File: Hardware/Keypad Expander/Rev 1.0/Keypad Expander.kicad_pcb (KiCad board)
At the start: 2 copper layers, 81.8 x 57.6 mm, 18 parts, among them J1 6502 Card Edge, J2 PORT B, J3 PORT A, U1 65C21, U2 AT28C64, U3 74HC138, U4 74HC138

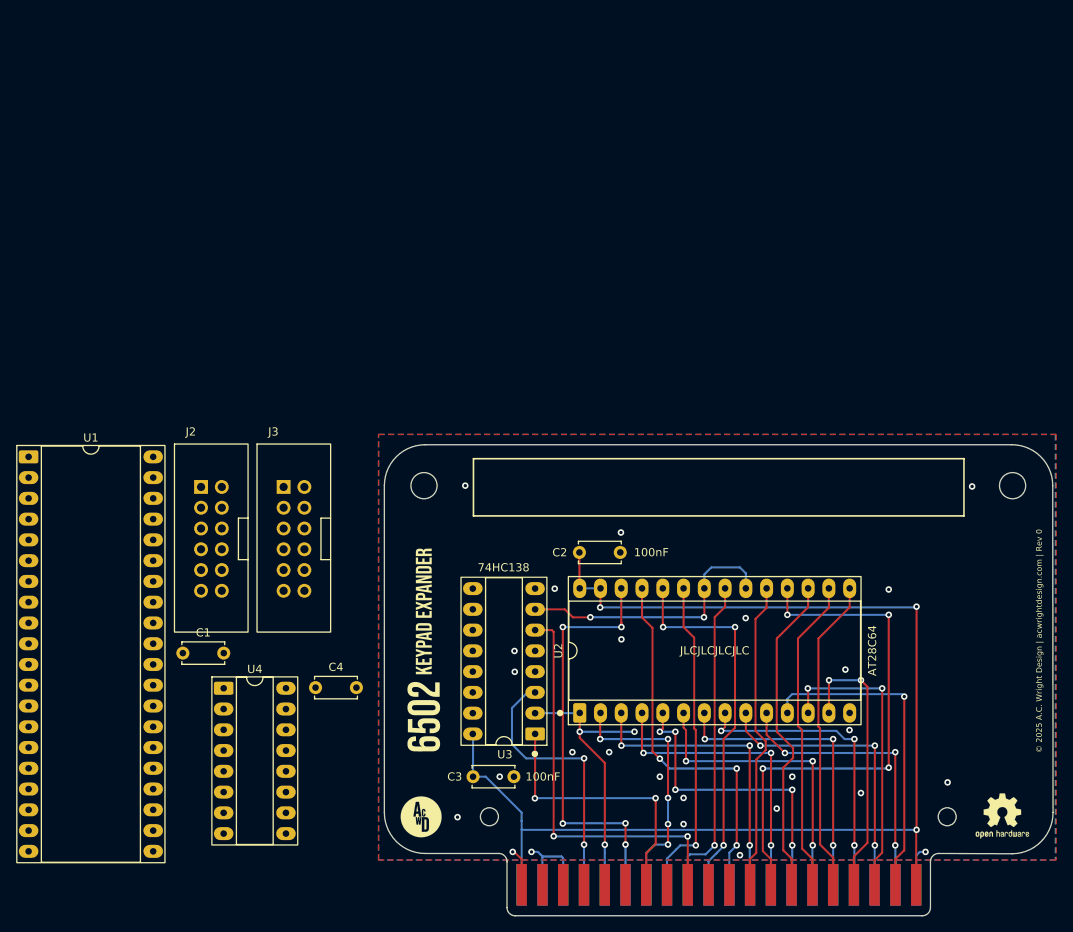
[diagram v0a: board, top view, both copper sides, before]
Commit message: Finish Keypad Expander layout
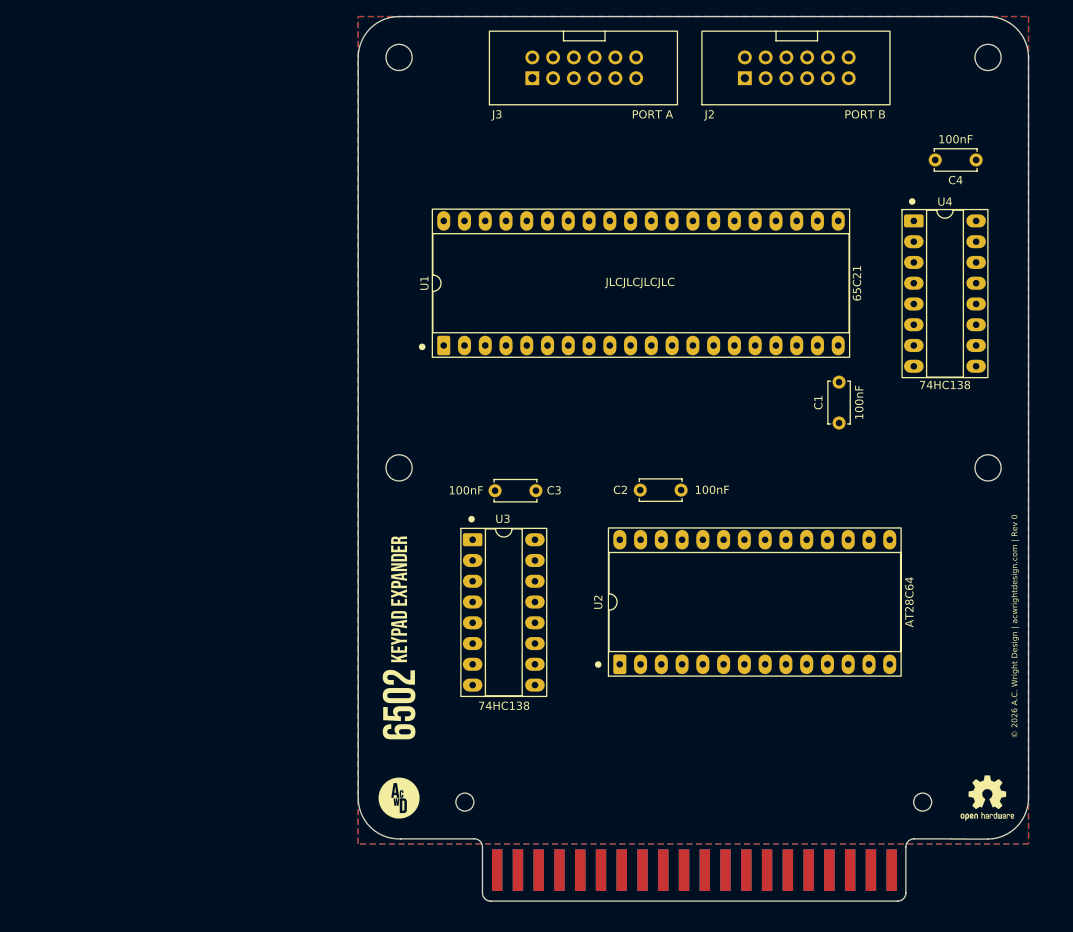
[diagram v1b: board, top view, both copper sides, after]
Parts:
- added H1: MountingHole, MountingHole:MountingHole_3.2mm_M3, F.Cu at (100.3, 28.8)
- added H2: MountingHole, MountingHole:MountingHole_3.2mm_M3, F.Cu at (172.3, 28.8)
- moved C4 103.4 mm to (170.9, 41.4), turned to 180 degrees
- moved U4 102.0 mm to (163.3, 48.8)
- moved C1 85.1 mm to (154.1, 73.5), turned to 90 degrees
- moved J2 83.2 mm to (142.6, 31.4), turned to 90 degrees
- moved J3 58.5 mm to (116.6, 31.4), turned to 90 degrees
- moved U1 52.6 mm to (105.8, 64.1), turned to 90 degrees
- moved C3 35.8 mm to (117.0, 81.8), turned to 180 degrees
- moved U3 25.0 mm to (109.3, 87.8), turned to 0 degrees
- moved C2 10.7 mm to (129.8, 81.7)
- moved U2 7.71 mm to (127.3, 103.1)
- moved H1 3.75 mm to (100.3, 79.0)
- moved H2 3.71 mm to (172.3, 79.0)
- moved G*** 3.55 mm to (100.3, 119.4)
- moved H3 3.49 mm to (108.3, 119.9)
- moved H4 3.49 mm to (164.3, 119.9)
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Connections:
- U1 pad 37: unconnected-(U1-IRQBB-Pad37) -> IRQB
- U3 pad 6: PHI2 -> VCC
- U4 pad 6: VCC -> PHI2
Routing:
- net VCC: track 152.2 -> 0.00 mm, vias 3 -> 0
- net D6: track 64.5 -> 0.00 mm, vias 4 -> 0
- net A13: track 51.4 -> 0.00 mm, vias 5 -> 0
- net PHI2: track 49.7 -> 0.00 mm, vias 2 -> 0
- net A9: track 46.5 -> 0.00 mm, vias 3 -> 0
- net A8: track 46.3 -> 0.00 mm, vias 3 -> 0
- net D0: track 39.9 -> 0.00 mm, vias 1 -> 0
- net D5: track 39.6 -> 0.00 mm
- net A11: track 39.5 -> 0.00 mm, vias 1 -> 0
- net A10: track 39.3 -> 0.00 mm, vias 1 -> 0
- net D3: track 38.6 -> 0.00 mm
- net D4: track 38.6 -> 0.00 mm
- net D7: track 38.1 -> 0.00 mm
- net A5: track 37.4 -> 0.00 mm, vias 5 -> 0
- net A2: track 37.0 -> 0.00 mm, vias 3 -> 0
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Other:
- board size 81.8 x 57.6 mm -> 82 x 108.2 mm
- board text added: "© 2026 A.C. Wright Design | acwrightdesign.com | Rev 0"
- board text removed: "© 2025 A.C. Wright Design | acwrightdesign.com | Rev 0"
